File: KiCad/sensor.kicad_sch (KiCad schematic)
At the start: 46 parts, among them J1 SKRKAEE020, J2 SKRKAEE020, J3 Conn_01x03_Male, U1 TCR2EF19, U2 LM3671MF 3.3, U3 PMW3360DM-T2QU, U4 RP2040, Y1 Crystal 3225 12MHz

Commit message: added license, some small tweaks and all.
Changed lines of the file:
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@@
   (paper "A3")
   (title_block
-    (date "2021-10-25")
+    (date "2021-10-30")
   )
   (junction (at 44.45 44.45) (diameter 1.016) (color 0 0 0 0))
@@
   )
   (text "2x 5.1K Resistors on the CC pins will = 5V@1.5A\nthis is the recomended default config for type-c"
-    (at 15.24 19.05 0)
+    (at 14.605 17.145 0)
     (effects (font (size 1.27 1.27)) (justify left bottom))
   )
@@
     (pin "3")
   )
-  (symbol (lib_id "logo:LOGO") (at 346.71 261.62 0) (unit 1)
-    (in_bom yes) (on_board yes)
-    (property "Reference" "#G1" (id 0) (at 346.71 266.2682 0)
+  (symbol (lib_id "logo:LOGO") (at 307.34 264.16 0) (unit 1)
+    (in_bom yes) (on_board yes)
+    (property "Reference" "#G1" (id 0) (at 307.34 268.8082 0)
       (effects (font (size 1.524 1.524)) hide)
     )
-    (property "Value" "LOGO" (id 1) (at 346.71 256.9718 0)
+    (property "Value" "LOGO" (id 1) (at 307.34 259.5118 0)
       (effects (font (size 1.524 1.524)) hide)
     )
-    (property "Footprint" "EnvExtras:logo" (id 2) (at 346.71 261.62 0)
-      (effects (font (size 1.27 1.27)) hide)
-    )
-    (property "Datasheet" "" (id 3) (at 346.71 261.62 0)
+    (property "Footprint" "EnvExtras:logo" (id 2) (at 307.34 264.16 0)
+      (effects (font (size 1.27 1.27)) hide)
+    )
+    (property "Datasheet" "" (id 3) (at 307.34 264.16 0)
       (effects (font (size 1.27 1.27)) hide)
     )
@@
     (pin "4")
   )
-  (symbol (lib_id "Graphic:Logo_Open_Hardware_Small") (at 359.41 262.89 0) (unit 1)
-    (in_bom yes) (on_board yes)
-    (property "Reference" "#LOGO1" (id 0) (at 359.41 255.905 0)
-      (effects (font (size 1.27 1.27)) hide)
-    )
-    (property "Value" "Logo_Open_Hardware_Small" (id 1) (at 359.41 268.605 0)
-      (effects (font (size 1.27 1.27)) hide)
-    )
-    (property "Footprint" "EnvExtras:logo" (id 2) (at 359.41 262.89 0)
-      (effects (font (size 1.27 1.27)) hide)
-    )
-    (property "Datasheet" "~" (id 3) (at 359.41 262.89 0)
-      (effects (font (size 1.27 1.27)) hide)
-    )
+  (symbol (lib_id "Graphic:Logo_Open_Hardware_Small") (at 321.31 262.89 0) (unit 1)
+    (in_bom yes) (on_board yes)
+    (property "Reference" "#LOGO1" (id 0) (at 321.31 255.905 0)
+      (effects (font (size 1.27 1.27)) hide)
+    )
+    (property "Value" "Logo_Open_Hardware_Small" (id 1) (at 321.31 268.605 0)
+      (effects (font (size 1.27 1.27)) hide)
+    )
+    (property "Footprint" "EnvExtras:logo" (id 2) (at 321.31 262.89 0)
+      (effects (font (size 1.27 1.27)) hide)
+    )
+    (property "Datasheet" "~" (id 3) (at 321.31 262.89 0)
+      (effects (font (size 1.27 1.27)) hide)
+    )

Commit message: Decided redo PCB
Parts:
- added SW1, SW2: MouseSwitch, MouseSwitch:MouseSwitch, symbol Switch:SW_Push_SPDT
- U2: footprint Package_TO_SOT_SMD:TSOT-23-5 -> Package_TO_SOT_SMD:SOT-23-5
- gave numbers to parts that had none: 3
- renumbered C9 to C10, C10 to C11, C11 to C12, C12 to C13, C13 to C14, C14 to C15, C15 to C16, C16 to C17, C17 to C18, C5 to C6, C6 to C7, C7 to C8, C8 to C9, R1 to R2, R2 to R4
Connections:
- net GPIO5: now also SW1.1 (A)
- net GPIO6: now also SW1.2 (B)
- net GPIO7: now also SW2.1 (A)
- net GPIO8: now also SW2.2 (B)

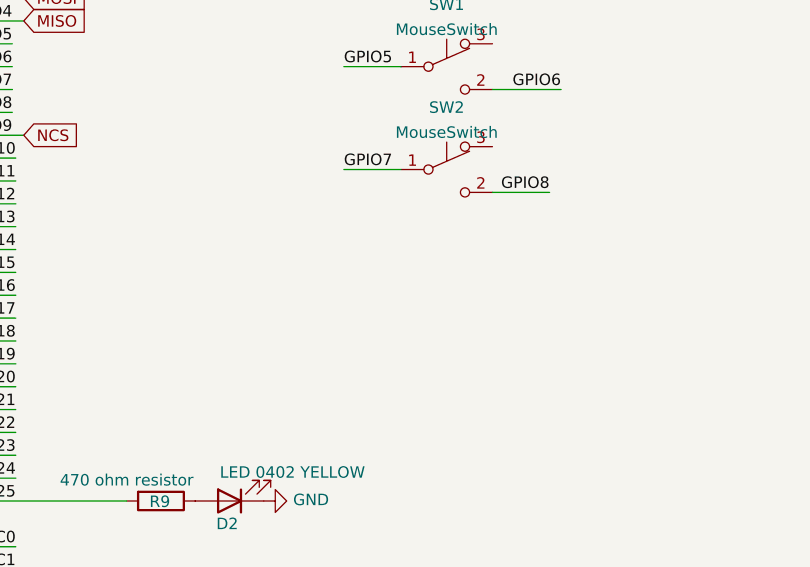
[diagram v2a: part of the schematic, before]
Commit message: added rotary encoder to the schematic
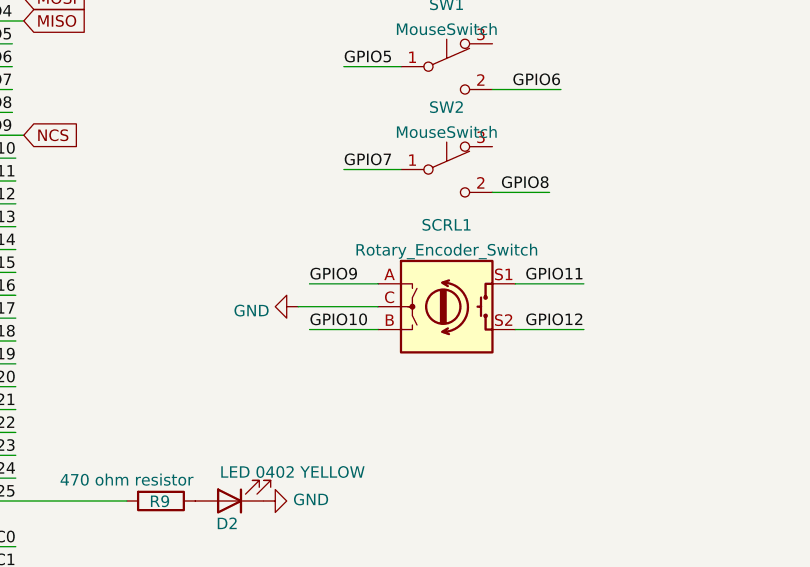
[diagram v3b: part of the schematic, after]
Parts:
- added SCRL1: Rotary_Encoder_Switch, symbol Device:Rotary_Encoder_Switch
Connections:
- net GND: now also SCRL1.C
- net GPIO10: now also SCRL1.B
- net GPIO11: now also SCRL1.S1
- net GPIO12: now also SCRL1.S2
- net NCS: now also SCRL1.A
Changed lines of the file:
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@@
     (stroke (width 0) (type solid) (color 0 0 0 0))
+  )
+  (wire (pts (xy 252.73 207.01) (xy 261.62 207.01))
+    (stroke (width 0) (type default) (color 0 0 0 0))
+  )
+  (wire (pts (xy 254 204.47) (xy 261.62 204.47))
+    (stroke (width 0) (type default) (color 0 0 0 0))
+  )
+  (wire (pts (xy 254 209.55) (xy 261.62 209.55))
+    (stroke (width 0) (type default) (color 0 0 0 0))
   )
   (wire (pts (xy 255.651 114.3) (xy 265.811 114.3))
@@
     (stroke (width 0) (type default) (color 0 0 0 0))
   )
+  (wire (pts (xy 276.86 204.47) (xy 284.48 204.47))
+    (stroke (width 0) (type default) (color 0 0 0 0))
+  )
+  (wire (pts (xy 276.86 209.55) (xy 284.48 209.55))
+    (stroke (width 0) (type default) (color 0 0 0 0))
+  )
   (polyline (pts (xy 78.74 15.24) (xy 156.21 15.24))
     (stroke (width 0) (type default) (color 0 0 0 0))
@@
     (effects (font (size 1.27 1.27)) (justify right bottom))
   )
+  (label "GPIO9" (at 254 204.47 0)
+    (effects (font (size 1.27 1.27)) (justify left bottom))
+  )
+  (label "GPIO10" (at 254 209.55 0)
+    (effects (font (size 1.27 1.27)) (justify left bottom))
+  )
   (label "GPIO5" (at 257.81 180.34 0)
     (effects (font (size 1.27 1.27)) (justify left bottom))
@@
   )
   (label "GPIO6" (at 281.94 182.88 180)
+    (effects (font (size 1.27 1.27)) (justify right bottom))
+  )
+  (label "GPIO11" (at 284.48 204.47 180)
+    (effects (font (size 1.27 1.27)) (justify right bottom))
+  )
+  (label "GPIO12" (at 284.48 209.55 180)
     (effects (font (size 1.27 1.27)) (justify right bottom))
   )
@@
     )
     (property "Datasheet" "" (id 3) (at 248.92 228.6 0)
+      (effects (font (size 1.27 1.27)) hide)
+    )
+    (pin "1")
+  )
+  (symbol (lib_id "power:GND") (at 252.73 207.01 270) (unit 1)
+    (in_bom yes) (on_board yes) (fields_autoplaced)
+    (property "Reference" "#PWR?" (id 0) (at 246.38 207.01 0)
+      (effects (font (size 1.27 1.27)) hide)
+    )
+    (property "Value" "GND" (id 1) (at 249.555 207.489 90)
+      (effects (font (size 1.27 1.27)) (justify right))
+    )
+    (property "Footprint" "" (id 2) (at 252.73 207.01 0)
+      (effects (font (size 1.27 1.27)) hide)
+    )
+    (property "Datasheet" "" (id 3) (at 252.73 207.01 0)
       (effects (font (size 1.27 1.27)) hide)
     )
@@
       (effects (font (size 1.27 1.27)) hide)
     )
+  )
+  (symbol (lib_id "Device:Rotary_Encoder_Switch") (at 269.24 207.01 0) (unit 1)
+    (in_bom yes) (on_board yes) (fields_autoplaced)
+    (property "Reference" "SCRL1" (id 0) (at 269.24 197.9635 0))
+    (property "Value" "Rotary_Encoder_Switch" (id 1) (at 269.24 200.7386 0))
+    (property "Footprint" "" (id 2) (at 265.43 202.946 0)
+      (effects (font (size 1.27 1.27)) hide)
+    )
+    (property "Datasheet" "~" (id 3) (at 269.24 200.406 0)
+      (effects (font (size 1.27 1.27)) hide)
+    )
+    (pin "A")
+    (pin "B")
+    (pin "C")
+    (pin "S1")
+    (pin "S2")
   )
   (symbol (lib_id "Regulator_Switching:LM3670MF") (at 107.95 38.1 0) (unit 1)
@@
       (reference "#PWR035") (unit 1) (value "GND") (footprint "")
     )
+    (path "/4cb3bc3e-7d29-4bec-8734-1e5c1a8bb60a"
+      (reference "#PWR?") (unit 1) (value "GND") (footprint "")
+    )
     (path "/00000000-0000-0000-0000-00005f09255d"
       (reference "C1") (unit 1) (value "10uf 0603 6.3V") (footprint "Capacitor_SMD:C_0603_1608Metric")
@@
       (reference "R10") (unit 1) (value "1K 0402") (footprint "Resistor_SMD:R_0402_1005Metric")
     )
+    (path "/ea1356c4-e418-4da5-9050-69c2e4083d51"
+      (reference "SCRL1") (unit 1) (value "Rotary_Encoder_Switch") (footprint "")
+    )
     (path "/798c83d4-bf59-4ae7-be16-94ab000014d2"
